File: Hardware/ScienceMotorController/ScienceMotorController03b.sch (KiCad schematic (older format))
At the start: 16 parts

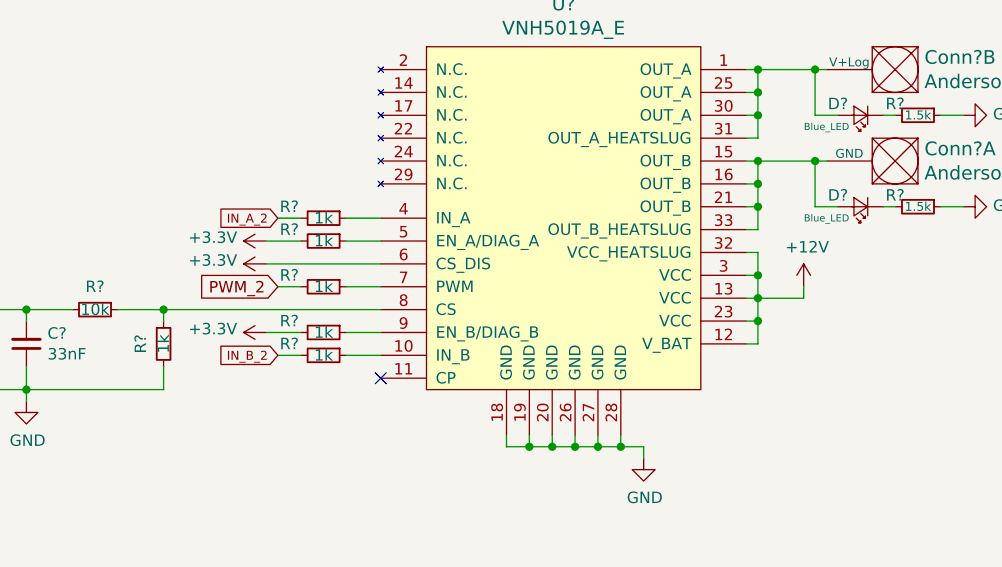
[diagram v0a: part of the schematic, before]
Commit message: changed everything to actuation, added schottky diode, added A/B flags to tiva
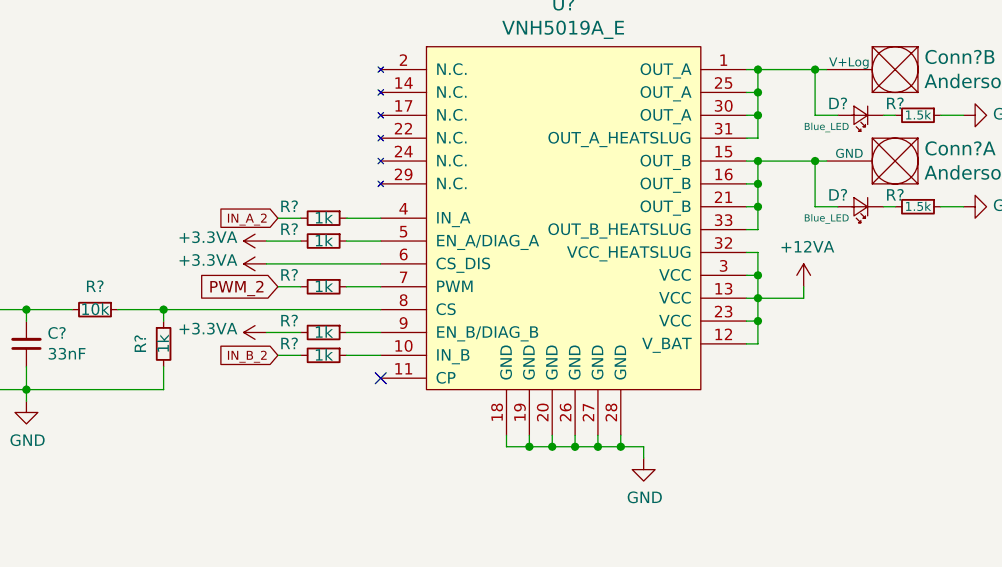
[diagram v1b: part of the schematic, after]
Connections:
- net +12V renamed +12VA
- net +3V3 renamed +3.3VA
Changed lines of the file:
@@
 	6550 4050 6550 3950
 Connection ~ 6550 3950
-$Comp
-L power:+12V #PWR?
-U 1 1 5FA5B75C
-P 6750 3800
-AR Path="/5F7D111E/5FA5B75C" Ref="#PWR?"  Part="1"
-AR Path="/5F7D111E/5FA36344/5FA5B75C" Ref="#PWR?"  Part="1"
-F 0 "#PWR?" H 6750 3650 50  0001 C CNN
-F 1 "+12V" H 6765 3973 50  0000 C CNN
-F 2 "" H 6750 3800 50  0001 C CNN
-F 3 "" H 6750 3800 50  0001 C CNN
-	1    6750 3800
-	1    0    0    -1
-$EndComp
 Wire Wire Line
 	6750 3800 6750 3850
@@
 Wire Wire Line
 	4550 4000 4400 4000
-$Comp
-L power:+3.3V #PWR?
-U 1 1 5FA5B79D
-P 4400 4000
-AR Path="/5F7D111E/5FA5B79D" Ref="#PWR?"  Part="1"
-AR Path="/5F7D111E/5FA36344/5FA5B79D" Ref="#PWR?"  Part="1"
-F 0 "#PWR?" H 4400 3850 50  0001 C CNN
-F 1 "+3.3V" V 4415 4128 50  0000 L CNN
-F 2 "" H 4400 4000 50  0001 C CNN
-F 3 "" H 4400 4000 50  0001 C CNN
-	1    4400 4000
-	0    -1   -1   0
-$EndComp
-$Comp
-L power:+3.3V #PWR?
-U 1 1 5FA5B7A3
-P 4400 3700
-AR Path="/5F7D111E/5FA5B7A3" Ref="#PWR?"  Part="1"
-AR Path="/5F7D111E/5FA36344/5FA5B7A3" Ref="#PWR?"  Part="1"
-F 0 "#PWR?" H 4400 3550 50  0001 C CNN
-F 1 "+3.3V" V 4415 3828 50  0000 L CNN
-F 2 "" H 4400 3700 50  0001 C CNN
-F 3 "" H 4400 3700 50  0001 C CNN
-	1    4400 3700
-	0    -1   -1   0
-$EndComp
 Wire Wire Line
 	4900 3700 4400 3700
@@
 Wire Wire Line
 	4900 3600 4750 3600
-$Comp
-L power:+3.3V #PWR?
-U 1 1 5FA5B7B1
-P 4400 3600
-AR Path="/5F7D111E/5FA5B7B1" Ref="#PWR?"  Part="1"
-AR Path="/5F7D111E/5FA36344/5FA5B7B1" Ref="#PWR?"  Part="1"
-F 0 "#PWR?" H 4400 3450 50  0001 C CNN
-F 1 "+3.3V" V 4415 3728 50  0000 L CNN
-F 2 "" H 4400 3600 50  0001 C CNN
-F 3 "" H 4400 3600 50  0001 C CNN
-	1    4400 3600
-	0    -1   -1   0
-$EndComp
 Wire Wire Line
 	4550 3600 4400 3600
@@
 Text Notes 7150 6900 0    197  ~ 0
 Sheet 03b: Motor Driver 2
+$Comp
+L power:+3.3VA #PWR?
+U 1 1 5F82EF15
+P 4400 3600
+F 0 "#PWR?" H 4400 3450 50  0001 C CNN
+F 1 "+3.3VA" V 4415 3727 50  0000 L CNN
+F 2 "" H 4400 3600 50  0001 C CNN
+F 3 "" H 4400 3600 50  0001 C CNN
+	1    4400 3600
+	0    -1   -1   0
+$EndComp
+$Comp
+L power:+3.3VA #PWR?
+U 1 1 5F82FC76
+P 4400 3700
+F 0 "#PWR?" H 4400 3550 50  0001 C CNN
+F 1 "+3.3VA" V 4415 3827 50  0000 L CNN
+F 2 "" H 4400 3700 50  0001 C CNN
+F 3 "" H 4400 3700 50  0001 C CNN
+	1    4400 3700
+	0    -1   -1   0
+$EndComp
+$Comp
+L power:+3.3VA #PWR?
+U 1 1 5F8301F0
+P 4400 4000
+F 0 "#PWR?" H 4400 3850 50  0001 C CNN
+F 1 "+3.3VA" V 4415 4127 50  0000 L CNN
+F 2 "" H 4400 4000 50  0001 C CNN
+F 3 "" H 4400 4000 50  0001 C CNN
+	1    4400 4000
+	0    -1   -1   0
+$EndComp
+$Comp
+L power:+12VA #PWR?
+U 1 1 5F830AA8
+P 6750 3800
+F 0 "#PWR?" H 6750 3650 50  0001 C CNN
+F 1 "+12VA" H 6765 3973 50  0000 C CNN
+F 2 "" H 6750 3800 50  0001 C CNN
+F 3 "" H 6750 3800 50  0001 C CNN
+	1    6750 3800
+	1    0    0    -1
+$EndComp
 $EndSCHEMATC

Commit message: fixed hierarchical
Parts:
- added FB? (x2): Ferrite_Bead, symbol Device:Ferrite_Bead_Small
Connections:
- net at U?.1 (OUT_A), U?.25 (OUT_A), U?.30 (OUT_A)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: now also FB?.2; no longer Conn?.2 (V+Log), D?.2 (A)
- net at U?.15 (OUT_B), U?.16 (OUT_B), U?.21 (OUT_B)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: now also FB?.2; no longer Conn?.1 (GND), D?.2 (A)
- net IN_A_2 renamed In_A_2
- net IN_B_2 renamed In_B_2
- new net: Conn?.2 (V+Log), D?.2 (A), FB?.1
- new net: Conn?.1 (GND), D?.2 (A), FB?.1
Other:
- moved on the sheet: Conn?A, Conn?B, D?, R?

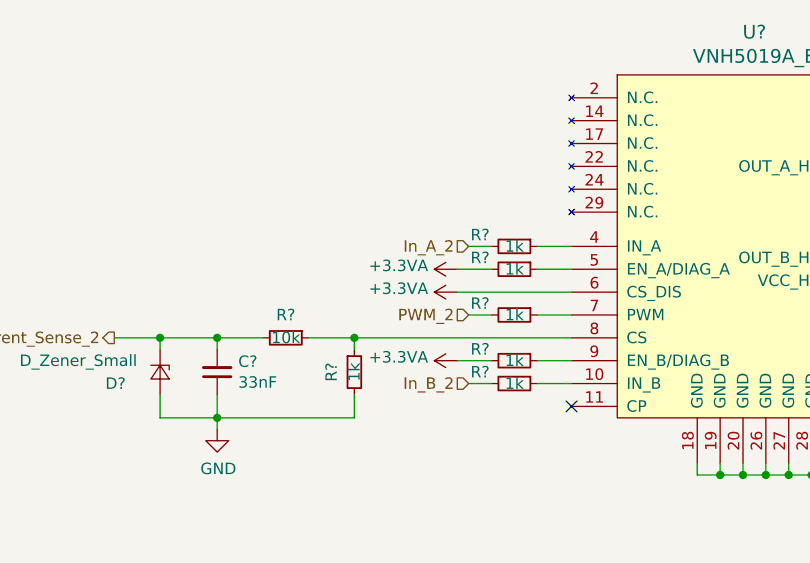
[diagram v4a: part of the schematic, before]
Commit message: Fixed 3.3V, added encoders
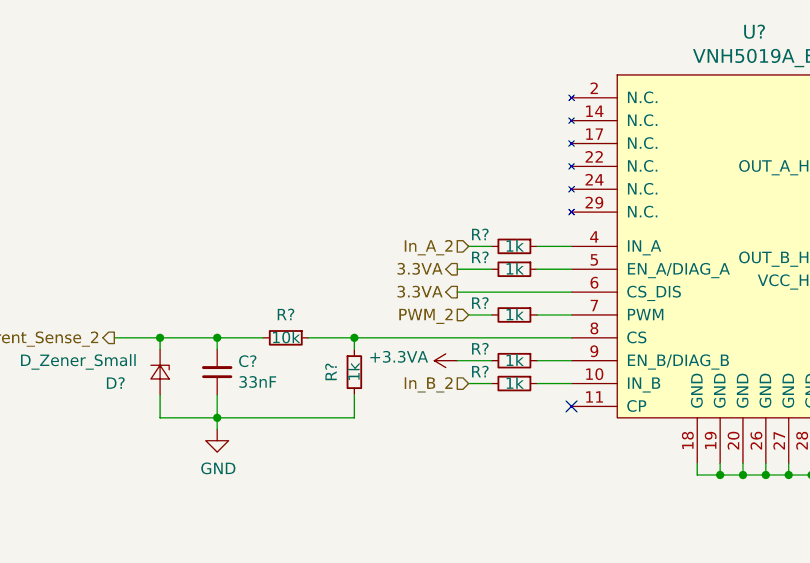
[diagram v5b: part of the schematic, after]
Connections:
- net +3.3VA: no longer R?.2, U?.6 (CS_DIS)
- new net 3.3VA: R?.2, U?.6 (CS_DIS)
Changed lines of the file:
@@
 $Descr A4 11693 8268
 encoding utf-8
-Sheet 4 10
+Sheet 4 11
 Title ""
 Date ""
@@
 $Comp
 L power:+3.3VA #PWR?
-U 1 1 5F82EF15
-P 4400 3600
-AR Path="/5F7D111E/5FA36344/5F82EF15" Ref="#PWR?"  Part="1"
-AR Path="/5F9082F8/5F82EF15" Ref="#PWR?"  Part="1"
-AR Path="/5F7148FA/5FA34AD5/5F82EF15" Ref="#PWR?"  Part="1"
-F 0 "#PWR?" H 4400 3450 50  0001 C CNN
-F 1 "+3.3VA" V 4415 3727 50  0000 L CNN
-F 2 "" H 4400 3600 50  0001 C CNN
-F 3 "" H 4400 3600 50  0001 C CNN
-	1    4400 3600
-	0    -1   -1   0
-$EndComp
-$Comp
-L power:+3.3VA #PWR?
-U 1 1 5F82FC76
-P 4400 3700
-AR Path="/5F7D111E/5FA36344/5F82FC76" Ref="#PWR?"  Part="1"
-AR Path="/5F9082F8/5F82FC76" Ref="#PWR?"  Part="1"
-AR Path="/5F7148FA/5FA34AD5/5F82FC76" Ref="#PWR?"  Part="1"
-F 0 "#PWR?" H 4400 3550 50  0001 C CNN
-F 1 "+3.3VA" V 4415 3827 50  0000 L CNN
-F 2 "" H 4400 3700 50  0001 C CNN
-F 3 "" H 4400 3700 50  0001 C CNN
-	1    4400 3700
-	0    -1   -1   0
-$EndComp
-$Comp
-L power:+3.3VA #PWR?
 U 1 1 5F8301F0
 P 4400 4000
@@
 Text HLabel 2900 3900 0    50   Output ~ 0
 Current_Sense_2
+Text HLabel 4400 3600 0    50   Output ~ 0
+3.3VA
+Text HLabel 4400 3700 0    50   Output ~ 0
+3.3VA
 $EndSCHEMATC

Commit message: added logic line
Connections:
- net 3.3VA is gone; now on net 3.3V: R?.2, U?.6 (CS_DIS)
- net +3.3VA renamed 3.3V
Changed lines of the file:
@@
 Sheet 03b: Motor Driver 2
-$Comp
-L power:+3.3VA #PWR?
-U 1 1 5F8301F0
-P 4400 4000
-AR Path="/5F7D111E/5FA36344/5F8301F0" Ref="#PWR?"  Part="1"
-AR Path="/5F9082F8/5F8301F0" Ref="#PWR?"  Part="1"
-AR Path="/5F7148FA/5FA34AD5/5F8301F0" Ref="#PWR?"  Part="1"
-F 0 "#PWR?" H 4400 3850 50  0001 C CNN
-F 1 "+3.3VA" V 4415 4127 50  0000 L CNN
-F 2 "" H 4400 4000 50  0001 C CNN
-F 3 "" H 4400 4000 50  0001 C CNN
-	1    4400 4000
-	0    -1   -1   0
-$EndComp
 $Comp
 L power:+12VA #PWR?
@@
 Current_Sense_2
 Text HLabel 4400 3600 0    50   Output ~ 0
-3.3VA
+3.3V
 Text HLabel 4400 3700 0    50   Output ~ 0
-3.3VA
+3.3V
+Text HLabel 4400 4000 0    50   Output ~ 0
+3.3V
 $EndSCHEMATC

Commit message: annotated
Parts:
- C3: renamed from C?; footprint (none) -> Capacitor_SMD:C_0603_1608Metric_Pad1.05x0.95mm_HandSolder
- gave numbers to parts that had none: 16
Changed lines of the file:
@@
 AR Path="/5F7D111E/5FA36344/5FA5B74A" Ref="U?"  Part="1"
 AR Path="/5F9082F8/5FA5B74A" Ref="U?"  Part="1"
-AR Path="/5F7148FA/5FA34AD5/5FA5B74A" Ref="U?"  Part="1"
-F 0 "U?" H 5700 5937 60  0000 C CNN
+AR Path="/5F7148FA/5FA34AD5/5FA5B74A" Ref="U3"  Part="1"
+F 0 "U3" H 5700 5937 60  0000 C CNN
 F 1 "VNH5019A_E" H 5700 5831 60  0000 C CNN
 F 2 "" H 5100 5550 60  0001 C CNN
@@
 AR Path="/5F7D111E/5FA36344/5FA5B767" Ref="R?"  Part="1"
 AR Path="/5F9082F8/5FA5B767" Ref="R?"  Part="1"
-AR Path="/5F7148FA/5FA34AD5/5FA5B767" Ref="R?"  Part="1"
-F 0 "R?" V 4600 3650 50  0000 C CNN
+AR Path="/5F7148FA/5FA34AD5/5FA5B767" Ref="R10"  Part="1"
+F 0 "R10" V 4600 3650 50  0000 C CNN
 F 1 "1k" V 4650 3800 50  0000 C CNN
 F 2 "" H 4650 3800 50  0001 C CNN
@@
 AR Path="/5F7D111E/5FA36344/5FA5B76D" Ref="R?"  Part="1"
 AR Path="/5F9082F8/5FA5B76D" Ref="R?"  Part="1"
-AR Path="/5F7148FA/5FA34AD5/5FA5B76D" Ref="R?"  Part="1"
-F 0 "R?" V 3850 4050 50  0000 C CNN
+AR Path="/5F7148FA/5FA34AD5/5FA5B76D" Ref="R7"  Part="1"
+F 0 "R7" V 3850 4050 50  0000 C CNN
 F 1 "1k" V 3950 4050 50  0000 C CNN
 F 2 "" H 3950 4050 50  0001 C CNN
@@
 AR Path="/5F7D111E/5FA36344/5FA5B773" Ref="C?"  Part="1"
 AR Path="/5F9082F8/5FA5B773" Ref="C?"  Part="1"
-AR Path="/5F7148FA/5FA34AD5/5FA5B773" Ref="C?"  Part="1"
-F 0 "C?" H 3258 4004 50  0000 R CNN
+AR Path="/5F7148FA/5FA34AD5/5FA5B773" Ref="C3"  Part="1"
+F 0 "C3" H 3258 4004 50  0000 R CNN
 F 1 "33nF" H 3258 4095 50  0000 R CNN
-F 2 "" H 3350 4050 50  0001 C CNN
+F 2 "Capacitor_SMD:C_0603_1608Metric_Pad1.05x0.95mm_HandSolder" H 3350 4050 50  0001 C CNN
 F 3 "~" H 3350 4050 50  0001 C CNN
 	1    3350 4050
@@
 AR Path="/5F7D111E/5FA36344/5FA5B779" Ref="D?"  Part="1"
 AR Path="/5F9082F8/5FA5B779" Ref="D?"  Part="1"
-AR Path="/5F7148FA/5FA34AD5/5FA5B779" Ref="D?"  Part="1"
-F 0 "D?" V 3150 3900 50  0000 R CNN
+AR Path="/5F7148FA/5FA34AD5/5FA5B779" Ref="D7"  Part="1"
+F 0 "D7" V 3150 3900 50  0000 R CNN
 F 1 "D_Zener_Small" V 3050 3950 50  0000 R CNN
 F 2 "" V 3100 4050 50  0001 C CNN
@@
 AR Path="/5F7D111E/5FA36344/5FA5B77F" Ref="R?"  Part="1"
 AR Path="/5F9082F8/5FA5B77F" Ref="R?"  Part="1"
-AR Path="/5F7148FA/5FA34AD5/5FA5B77F" Ref="R?"  Part="1"
-F 0 "R?" V 3550 3900 50  0000 C CNN
+AR Path="/5F7148FA/5FA34AD5/5FA5B77F" Ref="R6"  Part="1"
+F 0 "R6" V 3550 3900 50  0000 C CNN
 F 1 "10k" V 3650 3900 50  0000 C CNN
 F 2 "" H 3650 3900 50  0001 C CNN
@@
 AR Path="/5F7D111E/5FA36344/5FA5B795" Ref="R?"  Part="1"
 AR Path="/5F9082F8/5FA5B795" Ref="R?"  Part="1"
-AR Path="/5F7148FA/5FA34AD5/5FA5B795" Ref="R?"  Part="1"
-F 0 "R?" V 4600 3850 50  0000 C CNN
+AR Path="/5F7148FA/5FA34AD5/5FA5B795" Ref="R11"  Part="1"
+F 0 "R11" V 4600 3850 50  0000 C CNN
 F 1 "1k" V 4650 4000 50  0000 C CNN
 F 2 "" H 4650 4000 50  0001 C CNN
@@
 AR Path="/5F7D111E/5FA36344/5FA5B7AA" Ref="R?"  Part="1"
 AR Path="/5F9082F8/5FA5B7AA" Ref="R?"  Part="1"
-AR Path="/5F7148FA/5FA34AD5/5FA5B7AA" Ref="R?"  Part="1"
-F 0 "R?" V 4600 3450 50  0000 C CNN
+AR Path="/5F7148FA/5FA34AD5/5FA5B7AA" Ref="R9"  Part="1"
+F 0 "R9" V 4600 3450 50  0000 C CNN
 F 1 "1k" V 4650 3600 50  0000 C CNN
 F 2 "" H 4650 3600 50  0001 C CNN
@@
 AR Path="/5F7D111E/5FA36344/5FA5B7B8" Ref="R?"  Part="1"
 AR Path="/5F9082F8/5FA5B7B8" Ref="R?"  Part="1"
-AR Path="/5F7148FA/5FA34AD5/5FA5B7B8" Ref="R?"  Part="1"
-F 0 "R?" V 4600 3350 50  0000 C CNN
+AR Path="/5F7148FA/5FA34AD5/5FA5B7B8" Ref="R8"  Part="1"
+F 0 "R8" V 4600 3350 50  0000 C CNN
 F 1 "1k" V 4650 3500 50  0000 C CNN
 F 2 "" H 4650 3500 50  0001 C CNN
@@
 AR Path="/5F7D111E/5FA36344/5FA5B7C2" Ref="R?"  Part="1"
 AR Path="/5F9082F8/5FA5B7C2" Ref="R?"  Part="1"
-AR Path="/5F7148FA/5FA34AD5/5FA5B7C2" Ref="R?"  Part="1"
-F 0 "R?" V 4600 3950 50  0000 C CNN
+AR Path="/5F7148FA/5FA34AD5/5FA5B7C2" Ref="R12"  Part="1"
+F 0 "R12" V 4600 3950 50  0000 C CNN
 F 1 "1k" V 4650 4100 50  0000 C CNN
 F 2 "" H 4650 4100 50  0001 C CNN
@@
 AR Path="/5F7D111E/5FA36344/5FA5B7DA" Ref="#PWR?"  Part="1"
 AR Path="/5F9082F8/5FA5B7DA" Ref="#PWR?"  Part="1"
-AR Path="/5F7148FA/5FA34AD5/5FA5B7DA" Ref="#PWR?"  Part="1"
-F 0 "#PWR?" H 6050 4300 50  0001 C CNN
+AR Path="/5F7148FA/5FA34AD5/5FA5B7DA" Ref="#PWR017"  Part="1"
+F 0 "#PWR017" H 6050 4300 50  0001 C CNN
 F 1 "GND" H 6055 4377 50  0000 C CNN
 F 2 "" H 6050 4550 50  0001 C CNN
@@
 AR Path="/5F7D111E/5FA36344/5FA5B7E4" Ref="#PWR?"  Part="1"
 AR Path="/5F9082F8/5FA5B7E4" Ref="#PWR?"  Part="1"
-AR Path="/5F7148FA/5FA34AD5/5FA5B7E4" Ref="#PWR?"  Part="1"
-F 0 "#PWR?" H 3350 4050 50  0001 C CNN
+AR Path="/5F7148FA/5FA34AD5/5FA5B7E4" Ref="#PWR016"  Part="1"
+F 0 "#PWR016" H 3350 4050 50  0001 C CNN
 F 1 "GND" H 3355 4127 50  0000 C CNN
 F 2 "" H 3350 4300 50  0001 C CNN
@@
 AR Path="/5F7D111E/5FA36344/5FA5B7FC" Ref="Conn?"  Part="1"
 AR Path="/5F9082F8/5FA5B7FC" Ref="Conn?"  Part="1"
-AR Path="/5F7148FA/5FA34AD5/5FA5B7FC" Ref="Conn?"  Part="1"
-F 0 "Conn?" H 7672 3197 60  0000 R CNN
+AR Path="/5F7148FA/5FA34AD5/5FA5B7FC" Ref="Conn2"  Part="1"
+F 0 "Conn2" H 7672 3197 60  0000 R CNN
 F 1 "AndersonPP" H 7672 3303 60  0000 R CNN
 F 2 "" H 7550 2600 60  0001 C CNN
@@
 AR Path="/5F7D111E/5FA36344/5FA5B802" Ref="Conn?"  Part="2"
 AR Path="/5F9082F8/5FA5B802" Ref="Conn?"  Part="2"
-AR Path="/5F7148FA/5FA34AD5/5FA5B802" Ref="Conn?"  Part="2"
-F 0 "Conn?" H 7672 2797 60  0000 R CNN
+AR Path="/5F7148FA/5FA34AD5/5FA5B802" Ref="Conn2"  Part="2"
+F 0 "Conn2" H 7672 2797 60  0000 R CNN
 F 1 "AndersonPP" H 7672 2903 60  0000 R CNN
 F 2 "" H 7550 2200 60  0001 C CNN
@@
 AR Path="/5F7D111E/5FA36344/5FA5B816" Ref="D?"  Part="1"
 AR Path="/5F9082F8/5FA5B816" Ref="D?"  Part="1"
-AR Path="/5F7148FA/5FA34AD5/5FA5B816" Ref="D?"  Part="1"
-F 0 "D?" H 7550 3000 50  0000 C CNN
+AR Path="/5F7148FA/5FA34AD5/5FA5B816" Ref="D8"  Part="1"
+F 0 "D8" H 7550 3000 50  0000 C CNN
 F 1 "Blue_LED" H 7600 3100 31  0000 C CNN
 F 2 "" V 7450 3050 50  0001 C CNN
@@
 AR Path="/5F7D111E/5FA36344/5FA5B81C" Ref="D?"  Part="1"
 AR Path="/5F9082F8/5FA5B81C" Ref="D?"  Part="1"
-AR Path="/5F7148FA/5FA34AD5/5FA5B81C" Ref="D?"  Part="1"
-F 0 "D?" H 7550 3400 50  0000 C CNN
+AR Path="/5F7148FA/5FA34AD5/5FA5B81C" Ref="D9"  Part="1"
+F 0 "D9" H 7550 3400 50  0000 C CNN
 F 1 "Blue_LED" H 7600 3500 31  0000 C CNN
 F 2 "" V 7450 3450 50  0001 C CNN
@@
 AR Path="/5F7D111E/5FA36344/5FA5B822" Ref="R?"  Part="1"
 AR Path="/5F9082F8/5FA5B822" Ref="R?"  Part="1"
-AR Path="/5F7148FA/5FA34AD5/5FA5B822" Ref="R?"  Part="1"
-F 0 "R?" V 7650 3350 50  0000 C CNN
+AR Path="/5F7148FA/5FA34AD5/5FA5B822" Ref="R14"  Part="1"
+F 0 "R14" V 7650 3350 50  0000 C CNN
 F 1 "1.5k" V 7700 3450 39  0000 C CNN
 F 2 "" H 7700 3450 50  0001 C CNN
@@
 AR Path="/5F7D111E/5FA36344/5FA5B828" Ref="R?"  Part="1"
 AR Path="/5F9082F8/5FA5B828" Ref="R?"  Part="1"
-AR Path="/5F7148FA/5FA34AD5/5FA5B828" Ref="R?"  Part="1"
-F 0 "R?" V 7650 2950 50  0000 C CNN
+AR Path="/5F7148FA/5FA34AD5/5FA5B828" Ref="R13"  Part="1"
+F 0 "R13" V 7650 2950 50  0000 C CNN
 F 1 "1.5k" V 7700 3050 39  0000 C CNN
 F 2 "" H 7700 3050 50  0001 C CNN
@@
 AR Path="/5F7D111E/5FA36344/5FA5B830" Ref="#PWR?"  Part="1"
 AR Path="/5F9082F8/5FA5B830" Ref="#PWR?"  Part="1"
-AR Path="/5F7148FA/5FA34AD5/5FA5B830" Ref="#PWR?"  Part="1"
-F 0 "#PWR?" H 7900 2800 50  0001 C CNN
+AR Path="/5F7148FA/5FA34AD5/5FA5B830" Ref="#PWR019"  Part="1"
+F 0 "#PWR019" H 7900 2800 50  0001 C CNN
 F 1 "GND" V 7905 2922 50  0000 R CNN
 F 2 "" H 7900 3050 50  0001 C CNN
@@
 AR Path="/5F7D111E/5FA36344/5FA5B836" Ref="#PWR?"  Part="1"
 AR Path="/5F9082F8/5FA5B836" Ref="#PWR?"  Part="1"
-AR Path="/5F7148FA/5FA34AD5/5FA5B836" Ref="#PWR?"  Part="1"
-F 0 "#PWR?" H 7900 3200 50  0001 C CNN
+AR Path="/5F7148FA/5FA34AD5/5FA5B836" Ref="#PWR020"  Part="1"
+F 0 "#PWR020" H 7900 3200 50  0001 C CNN
 F 1 "GND" V 7905 3322 50  0000 R CNN
 F 2 "" H 7900 3450 50  0001 C CNN
@@
 AR Path="/5F7D111E/5FA36344/5F830AA8" Ref="#PWR?"  Part="1"
 AR Path="/5F9082F8/5F830AA8" Ref="#PWR?"  Part="1"
-AR Path="/5F7148FA/5FA34AD5/5F830AA8" Ref="#PWR?"  Part="1"
-F 0 "#PWR?" H 6750 3650 50  0001 C CNN
+AR Path="/5F7148FA/5FA34AD5/5F830AA8" Ref="#PWR018"  Part="1"
+F 0 "#PWR018" H 6750 3650 50  0001 C CNN
 F 1 "+12VA" H 6765 3973 50  0000 C CNN
 F 2 "" H 6750 3800 50  0001 C CNN
@@
 P 6900 2850
 AR Path="/5F9082F8/5F9D0A4B" Ref="FB?"  Part="1"
-AR Path="/5F7148FA/5FA34AD5/5F9D0A4B" Ref="FB?"  Part="1"
-F 0 "FB?" V 6663 2850 50  0000 C CNN
+AR Path="/5F7148FA/5FA34AD5/5F9D0A4B" Ref="FB1"  Part="1"
+F 0 "FB1" V 6663 2850 50  0000 C CNN
 F 1 "Ferrite_Bead" V 6754 2850 50  0000 C CNN
 F 2 "" V 6830 2850 50  0001 C CNN
@@
 P 6900 3250
 AR Path="/5F9082F8/5F9D10E3" Ref="FB?"  Part="1"
-AR Path="/5F7148FA/5FA34AD5/5F9D10E3" Ref="FB?"  Part="1"
-F 0 "FB?" V 6663 3250 50  0000 C CNN
+AR Path="/5F7148FA/5FA34AD5/5F9D10E3" Ref="FB2"  Part="1"
+F 0 "FB2" V 6663 3250 50  0000 C CNN
 F 1 "Ferrite_Bead" V 6754 3250 50  0000 C CNN
 F 2 "" V 6830 3250 50  0001 C CNN
